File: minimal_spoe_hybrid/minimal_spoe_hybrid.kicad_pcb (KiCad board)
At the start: 4 copper layers, 43.2 x 18.3 mm, 14 parts, among them J1 TBP02R2-381-03BE, J3 CLP-103-02-G-D-BE

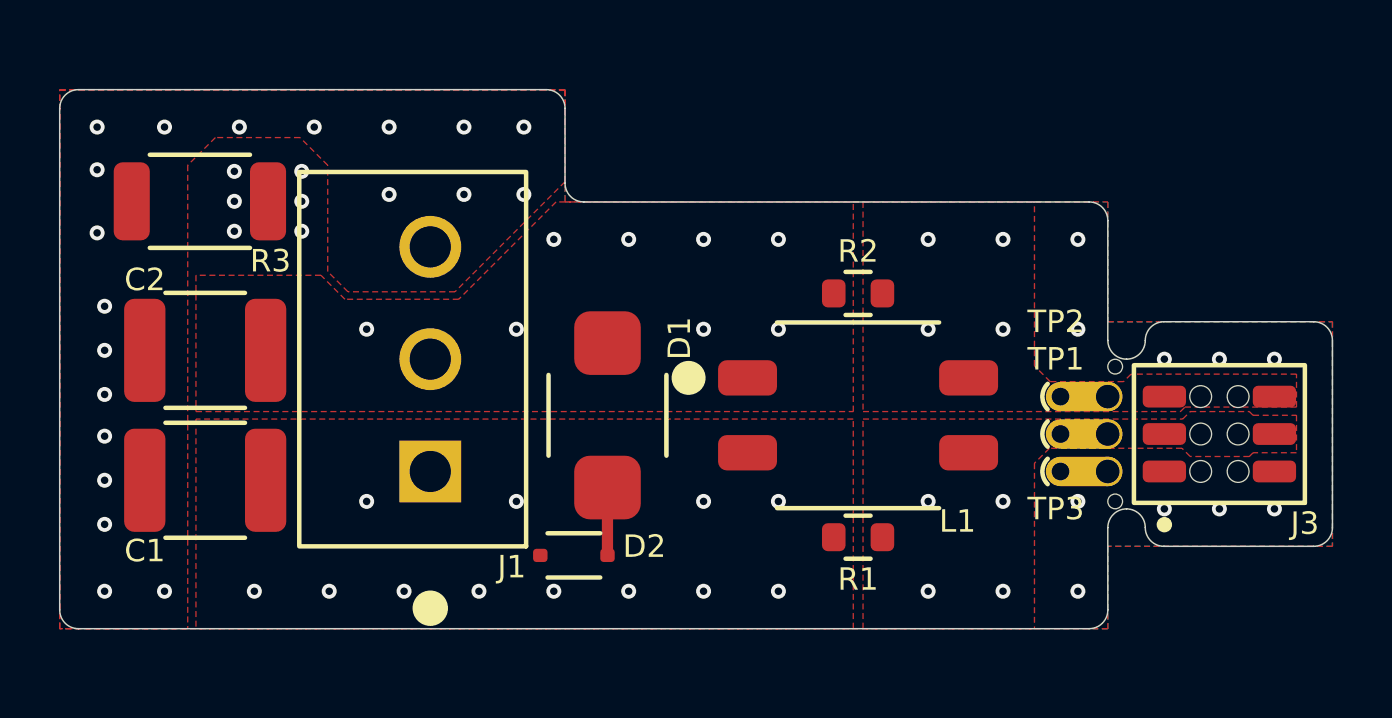
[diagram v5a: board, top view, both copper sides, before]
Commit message: Add minimal_spoe_hybrid.glb and update KiCAD Symbol Generator submodule
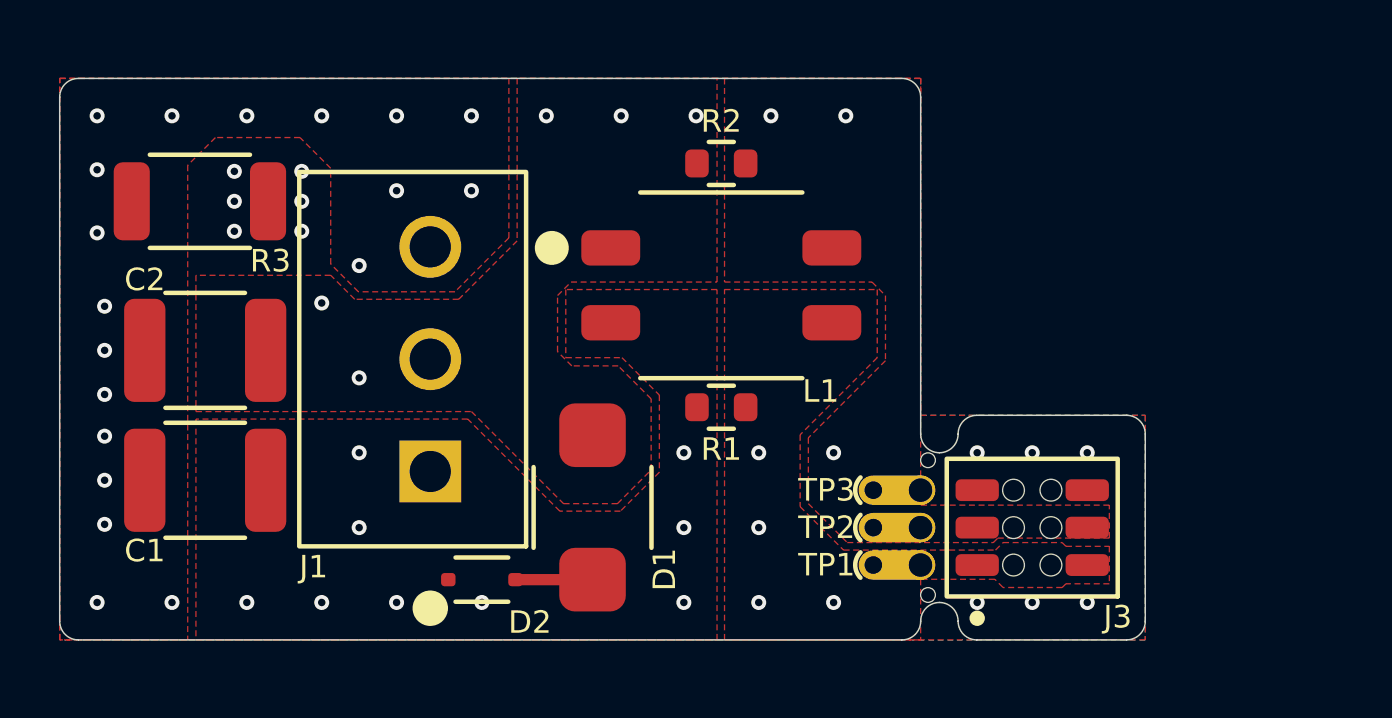
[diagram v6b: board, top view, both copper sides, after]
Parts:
- moved TP2 7.75 mm to (145.8, 114.4)
- moved TP1 7.75 mm to (145.8, 115.7)
- moved MB1 7.10 mm to (146.4, 114.4)
- moved J3 7.10 mm to (149.6, 114.4)
- moved L1 6.40 mm to (139.0, 106.2)
- moved R1 6.40 mm to (139.0, 110.3)
- moved R2 6.40 mm to (139.0, 102.0)
- moved TP3 6.38 mm to (145.8, 113.1)
- moved D2 3.23 mm to (130.9, 116.2)
- moved D1 3.17 mm to (134.7, 113.7)
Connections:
- J3 pad 1: GND -> /DATA_AND_POWER_P
- J3 pad 2: GND -> /DATA_AND_POWER_P
- J3 pad 3: /DATA_AND_POWER_P -> /DATA_AND_POWER_N
- J3 pad 4: /DATA_AND_POWER_P -> /DATA_AND_POWER_N
- J3 pad 5: /DATA_AND_POWER_N -> GND
- J3 pad 6: /DATA_AND_POWER_N -> GND
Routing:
- net GND: vias 44 -> 33
- net Earth: vias 20 -> 19
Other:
- board size 43.2 x 18.3 mm -> 36.8 x 19 mm

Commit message: Backup
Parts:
- moved D1 11.9 mm to (136.5, 102.0), turned to 0 degrees
- moved MB1 11.7 mm to (149.0, 103.0)
- moved TP2 11.7 mm to (148.3, 103.0)
- moved TP3 11.7 mm to (148.3, 101.7)
- moved J3 11.7 mm to (152.1, 103.0)
- moved TP1 11.7 mm to (148.3, 104.2)
- moved D2 8.50 mm to (133.4, 108.0), turned to 90 degrees
- moved R1 3.35 mm to (142.1, 111.5)
- moved R2 3.35 mm to (142.1, 103.3)
- moved L1 1.62 mm to (140.1, 107.4)
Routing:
- net Net-(D1-Pad1): track 2.61 -> 5.07 mm
- net GND: vias 33 -> 19
- net Earth: vias 19 -> 18
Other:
- board size 36.8 x 19 mm -> 39.4 x 19 mm

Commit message: Update KiCAD Symbols Generator submodule to latest commit
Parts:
- J1: value TBP02R2-381-03BE -> TBP02R2-381
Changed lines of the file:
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@@
 		)
 		(property "Footprint" "resistor_footprints:R_0603_1608Metric"
-			(at 0 0 360)
+			(at 0 0 0)
 			(layer "F.Fab")
 			(hide yes)
@@
 		)
 		(property "Datasheet" "https://industrial.panasonic.com/cdbs/www-data/pdf/RDA0000/AOA0000C304.pdf"
-			(at 0 0 360)
+			(at 0 0 0)
 			(layer "F.Fab")
 			(hide yes)
@@
 		)
 		(property "Description" "RES SMD 10 kΩ 1% 0603 75V"
-			(at 0 0 360)
+			(at 0 0 0)
 			(layer "F.Fab")
 			(hide yes)
@@
 		)
 		(model "${KIPRJMOD}/KiCAD_Symbol_Generator/3D_models/R_0603.step"
+			(hide yes)
+			(offset
+				(xyz 0 0 0)
+			)
+			(scale
+				(xyz 1 1 1)
+			)
+			(rotate
+				(xyz 0 0 0)
+			)
+		)
+		(model "${3D_MODELS_VAULT}/3D_models/resistors/R_0603.step"
 			(offset
 				(xyz 0 0 0)
@@
 		)
 		(model "${KIPRJMOD}/KiCAD_Symbol_Generator/3D_models/R_2010.step"
+			(hide yes)
+			(offset
+				(xyz 0 0 0)
+			)
+			(scale
+				(xyz 1 1 1)
+			)
+			(rotate
+				(xyz 0 0 0)
+			)
+		)
+		(model "${3D_MODELS_VAULT}/3D_models/resistors/R_2010.step"
 			(offset
 				(xyz 0 0 0)
@@
 		)
 		(model "${KIPRJMOD}/KiCAD_Symbol_Generator/3D_models/C_1812.step"
+			(hide yes)
+			(offset
+				(xyz 0 0 0)
+			)
+			(scale
+				(xyz 1 1 1)
+			)
+			(rotate
+				(xyz 0 0 0)
+			)
+		)
+		(model "${3D_MODELS_VAULT}/3D_models/capacitors/C_1812.step"
 			(offset
 				(xyz 0 0 0)
@@
 		)
 		(property "Footprint" "coupled_inductor_footprints:SRF0905A"
-			(at 0 0 360)
+			(at 0 0 0)
 			(layer "F.Fab")
 			(hide yes)
@@
 		)
 		(property "Datasheet" "https://bourns.com/docs/product-datasheets/srf0905a.pdf"
-			(at 0 0 360)
+			(at 0 0 0)
 			(layer "F.Fab")
 			(hide yes)
@@
 		)
 		(property "Description" "COUPLED INDUCTOR SMD 470 µH ±20%"
-			(at 0 0 360)
+			(at 0 0 0)
 			(layer "F.Fab")
 			(hide yes)
@@
 		)
 		(model "${KIPRJMOD}/KiCAD_Symbol_Generator/3D_models/SRF0905A.step"
+			(hide yes)
+			(offset
+				(xyz 0 0 0)
+			)
+			(scale
+				(xyz 1 1 1)
+			)
+			(rotate
+				(xyz 0 0 0)
+			)
+		)
+		(model "${3D_MODELS_VAULT}/3D_models/coupled_inductors/SRF0905A.step"
 			(offset
 				(xyz 0 0 0)
@@
 		)
 		(model "${KIPRJMOD}/KiCAD_Symbol_Generator/3D_models/C_1812.step"
+			(hide yes)
+			(offset
+				(xyz 0 0 0)
+			)
+			(scale
+				(xyz 1 1 1)
+			)
+			(rotate
+				(xyz 0 0 0)
+			)
+		)
+		(model "${3D_MODELS_VAULT}/3D_models/capacitors/C_1812.step"
 			(offset
 				(xyz 0 0 0)
@@
 		)
 		(property "Footprint" "resistor_footprints:R_0603_1608Metric"
-			(at 0 0 360)
+			(at 0 0 0)
 			(layer "F.Fab")
 			(hide yes)
@@
 		)
 		(property "Datasheet" "https://industrial.panasonic.com/cdbs/www-data/pdf/RDA0000/AOA0000C304.pdf"
-			(at 0 0 360)
+			(at 0 0 0)
 			(layer "F.Fab")
 			(hide yes)
@@
 		)
 		(property "Description" "RES SMD 10 kΩ 1% 0603 75V"
-			(at 0 0 360)
+			(at 0 0 0)
 			(layer "F.Fab")
 			(hide yes)
@@
 		)
 		(model "${KIPRJMOD}/KiCAD_Symbol_Generator/3D_models/R_0603.step"
+			(hide yes)
+			(offset
+				(xyz 0 0 0)
+			)
+			(scale
+				(xyz 1 1 1)
+			)
+			(rotate
+				(xyz 0 0 0)
+			)
+		)
+		(model "${3D_MODELS_VAULT}/3D_models/resistors/R_0603.step"
 			(offset
 				(xyz 0 0 0)
@@
 			(net 6 "/DATA_AND_POWER_P")
 			(pintype "unspecified")
-			(zone_connect 2)
 			(teardrops
 				(best_length_ratio 0.5)
@@
 			(net 6 "/DATA_AND_POWER_P")
 			(pintype "unspecified")
-			(zone_connect 2)
 			(teardrops
 				(best_length_ratio 0.5)
@@
 			(net 5 "/DATA_AND_POWER_N")
 			(pintype "unspecified")
-			(zone_connect 2)
 			(teardrops
 				(best_length_ratio 0.5)
@@
 			(net 5 "/DATA_AND_POWER_N")
 			(pintype "unspecified")
-			(zone_connect 2)
 			(teardrops
 				(best_length_ratio 0.5)
@@
 			(net 4 "GND")
 			(pintype "unspecified")
-			(zone_connect 2)
 			(teardrops
 				(best_length_ratio 0.5)
@@
 			(net 4 "GND")
 			(pintype "unspecified")
-			(zone_connect 2)
 			(teardrops
 				(best_length_ratio 0.5)
@@
 		)
 		(model "${KIPRJMOD}/KiCAD_Symbol_Generator/3D_models/CLP-103-02-G-D-BE.step"
+			(hide yes)
+			(offset
+				(xyz 0 0 0)
+			)
+			(scale
+				(xyz 1 1 1)
+			)
+			(rotate
+				(xyz 0 0 0)
+			)
+		)
+		(model "${3D_MODELS_VAULT}/3D_models/connectors/CLP-103-02-G-D-BE.step"
 			(offset
 				(xyz 0 0 0)
@@
 			)
 		)
-		(property "Value" "TBP02R2-381-03BE"
+		(property "Value" "TBP02R2-381"
 			(at 0 -6.8 90)
 			(unlocked yes)
@@
 			(pintype "unspecified")
 			(solder_mask_margin 0.102)
-			(zone_connect 2)
 			(teardrops
 				(best_length_ratio 0.5)
@@
 			(pintype "unspecified")
 			(solder_mask_margin 0.102)
-			(zone_connect 2)
 			(teardrops
 				(best_length_ratio 0.5)
@@
 			(pintype "unspecified")
 			(solder_mask_margin 0.102)
-			(zone_connect 2)
 			(teardrops
 				(best_length_ratio 0.5)
@@
 		)
 		(model "${KIPRJMOD}/KiCAD_Symbol_Generator/3D_models/CUI_DEVICES_TBP02R2-381-03BE.step"
+			(hide yes)
+			(offset
+				(xyz 0 0 0)
+			)
+			(scale
+				(xyz 1 1 1)
+			)
+			(rotate
+				(xyz 0 0 0)
+			)
+		)
+		(model "${3D_MODELS_VAULT}/3D_models/connectors/CUI_DEVICES_TBP02R2-381-03BE.step"
 			(offset
 				(xyz 0 0 0)
@@
 		)
 		(property "Footprint" "diode_footprints:DO-214AA"
-			(at 0 0 360)
+			(at 0 0 0)
 			(layer "F.Fab")
 			(hide yes)
@@
 		)
 		(property "Datasheet" "https://www.littelfuse.com/assetdocs/tvs-diodes-smbj-series-datasheet?assetguid=09a6ae9a-73cb-4ac4-acac-e6dab92ab953"
-			(at 0 0 360)
+			(at 0 0 0)
 			(layer "F.Fab")
 			(hide yes)
@@
 		)
 		(property "Description" "Bidirectional TVS SMD 58 V"
-			(at 0 0 360)
+			(at 0 0 0)
 			(layer "F.Fab")
 			(hide yes)
@@
 			)
 		)
-		(model "${KIPRJMOD}/KiCAD_Symbol_Generator/3D_models/DO-214AA.step"
+		(model "KiCAD_Symbol_Generator/3D_models/DO-214AA.step"
+			(hide yes)
+			(offset
+				(xyz 0 0 0)
+			)
+			(scale
+				(xyz 1 1 1)
+			)
+			(rotate
+				(xyz 0 0 0)
+			)
+		)
+		(model "${3D_MODELS_VAULT}/3D_models/diodes/DO-214AA.step"
 			(offset
 				(xyz 0 0 0)
@@
 			(layer "F.Fab")
 		)
-		(fp_poly
-			(pts
-				(xy 0.49 0) (xy 1.14 0) (xy 0.49 0) (xy 0.49 0.225) (xy 0 0) (xy 0 0.225) (xy 0 0) (xy -1.14 0)
-				(xy 0 0) (xy 0 -0.225) (xy 0 0) (xy 0.49 -0.225)
-			)
-			(stroke
-				(width 0.1)
-				(type solid)
-			)
-			(fill solid)
-			(layer "F.Fab")
-		)
 		(fp_text user "${REFERENCE}"
 			(at 0 4.064 90)
@@
 			)
 		)
-		(model "${KIPRJMOD}/KiCAD_Symbol_Generator/3D_models/SOD323.step"
+		(model "KiCAD_Symbol_Generator/3D_models/SOD323.step"
+			(hide yes)
+			(offset
+				(xyz 0 0 0)
+			)
+			(scale
+				(xyz 1 1 1)
+			)
+			(rotate
+				(xyz 0 0 0)
+			)
+		)
+		(model "${3D_MODELS_VAULT}/3D_models/diodes/SOD323.step"
 			(offset
 				(xyz 0 0 0)
@@
 		(name "$teardrop_padvia$")
 		(hatch full 0.1)
+		(priority 30001)
+		(attr
+			(teardrop
+				(type padvia)
+			)
+		)
+		(connect_pads yes
+			(clearance 0)
+		)
+		(min_thickness 0.0254)
+		(filled_areas_thickness no)
+		(fill yes
+			(thermal_gap 0.5)
+			(thermal_bridge_width 0.5)
+			(island_removal_mode 1)
+			(island_area_min 10)
+		)
+		(polygon
+			(pts
+				(xy 133.567821 106.411176) (xy 133.518815 106.464968) (xy 133.46981 106.516691) (xy 133.420805 106.566344)
+				(xy 133.3718 106.613927) (xy 133.322795 106.65944) (xy 133.41444 106.905306) (xy 133.63994 106.983461)
+				(xy 133.691506 106.902964) (xy 133.743073 106.824537) (xy 133.79464 106.74818) (xy 133.846207 106.673893)
+				(xy 133.897774 106.601677)
+			)
+		)
+	)
+	(zone
+		(net 7)
+		(net_name "Net-(D1-Pad1)")
+		(layer "F.Cu")
+		(name "$teardrop_padvia$")
+		(hatch full 0.1)
 		(priority 30000)
 		(attr
@@
 			)
 		)
-	)
-	(zone
-		(net 7)
-		(net_name "Net-(D1-Pad1)")
-		(layer "F.Cu")
-		(name "$teardrop_padvia$")
-		(hatch full 0.1)
-		(priority 30001)
-		(attr
-			(teardrop
-				(type padvia)
-			)
-		)
-		(connect_pads yes
-			(clearance 0)
-		)
-		(min_thickness 0.0254)
-		(filled_areas_thickness no)
-		(fill yes
-			(thermal_gap 0.5)
-			(thermal_bridge_width 0.5)
-			(island_removal_mode 1)
-			(island_area_min 10)
-		)
-		(polygon
-			(pts
-				(xy 133.567821 106.411176) (xy 133.518815 106.464968) (xy 133.46981 106.516691) (xy 133.420805 106.566344)
-				(xy 133.3718 106.613927) (xy 133.322795 106.65944) (xy 133.41444 106.905306) (xy 133.63994 106.983461)
-				(xy 133.691506 106.902964) (xy 133.743073 106.824537) (xy 133.79464 106.74818) (xy 133.846207 106.673893)
-				(xy 133.897774 106.601677)
-			)
-		)
